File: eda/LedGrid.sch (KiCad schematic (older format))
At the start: 99 parts

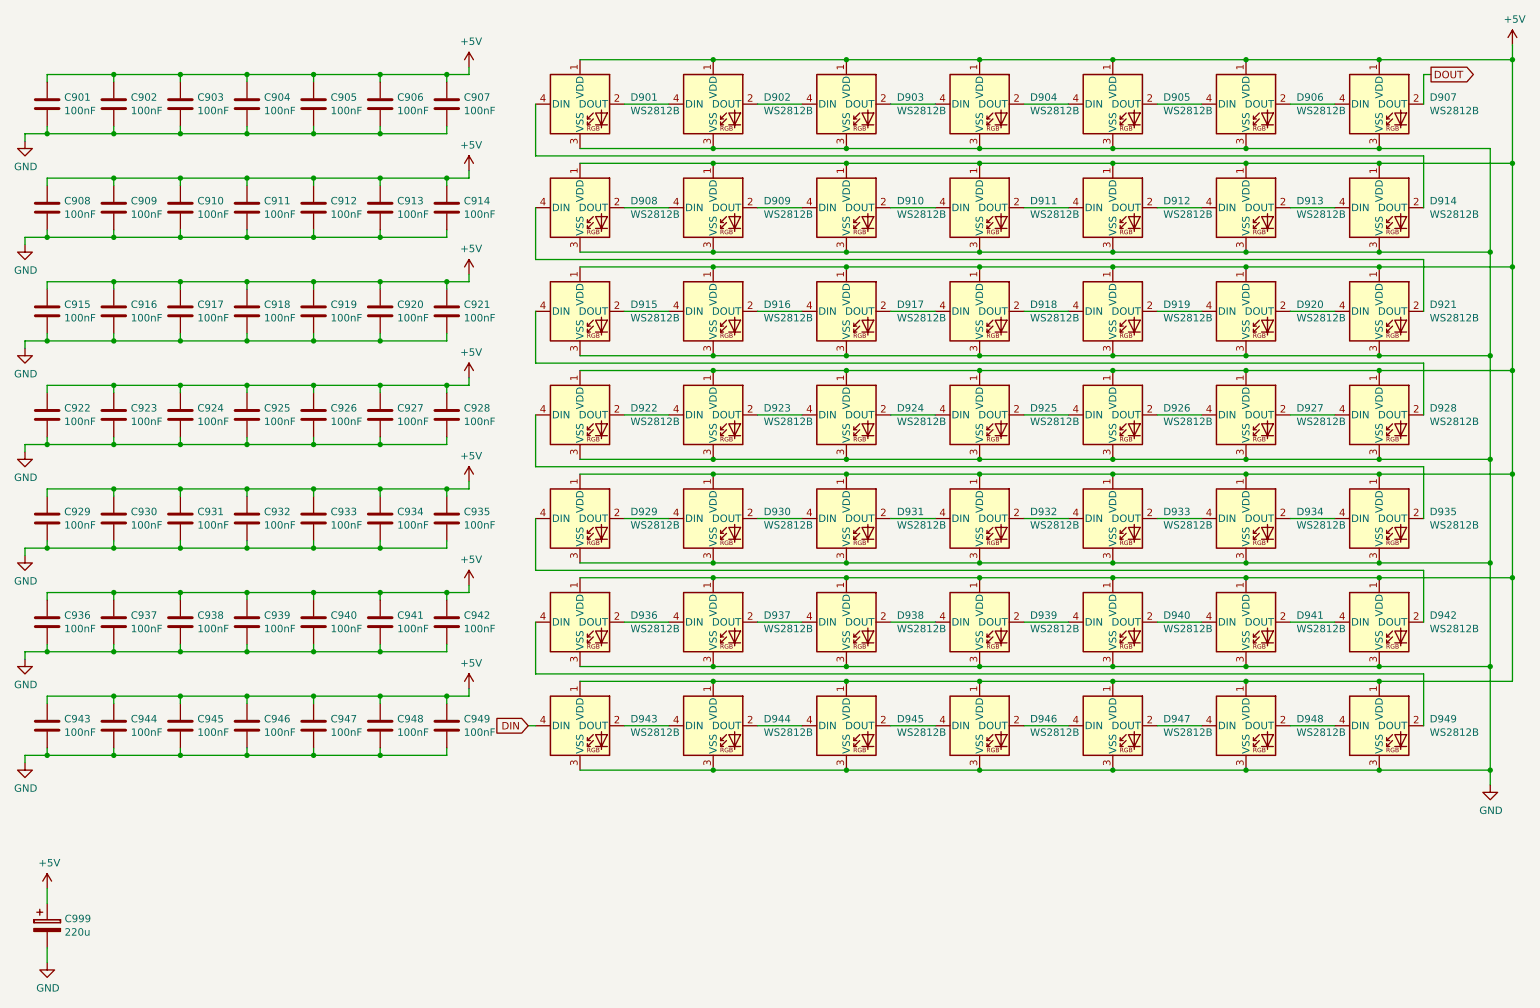
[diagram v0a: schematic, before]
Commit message: WS2812B grid finished
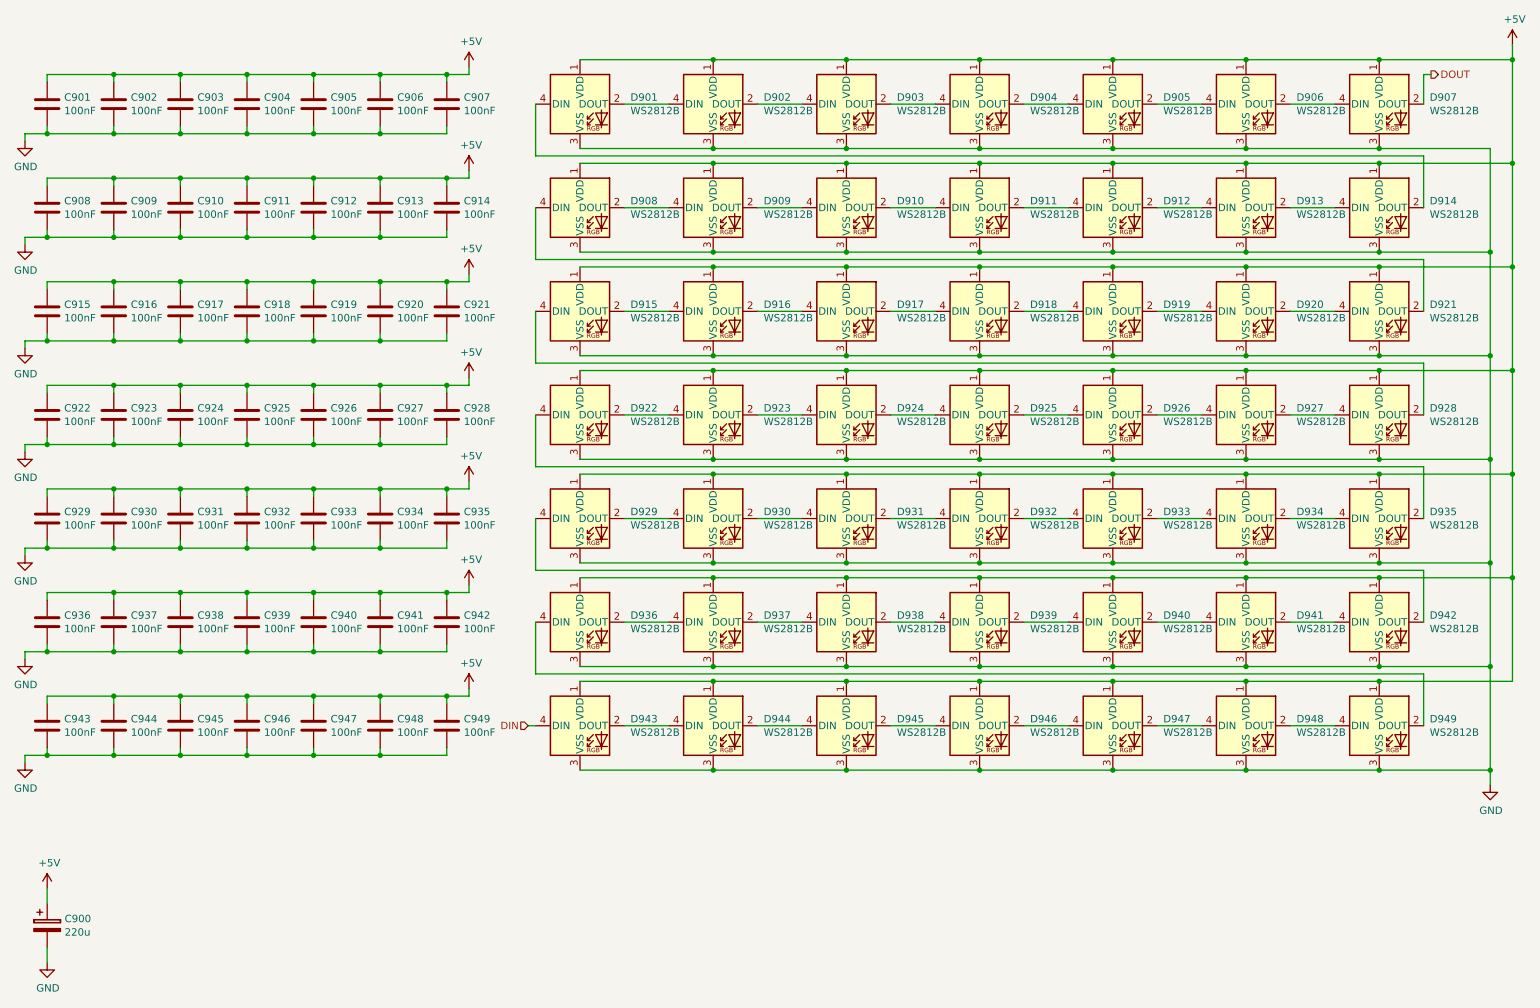
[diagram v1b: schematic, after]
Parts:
- C902, C903, C904, C905, C906, C907, C908, C909, C910, C911, C912, C913, C914, C915, C916, C917, C918, C919, C920, C921, C922, C923, C924, C925, C926, C927, C928, C929, C930, C931, C932, C933, C934, C935, C936, C937, C938, C939, C940, C941, C942, C943, C944, C945, C946, C947, C948, C949: footprint Capacitor_SMD:CP_Elec_6.3x5.3 -> Capacitor_SMD:C_0603_1608Metric
- renumbered C999 to C900

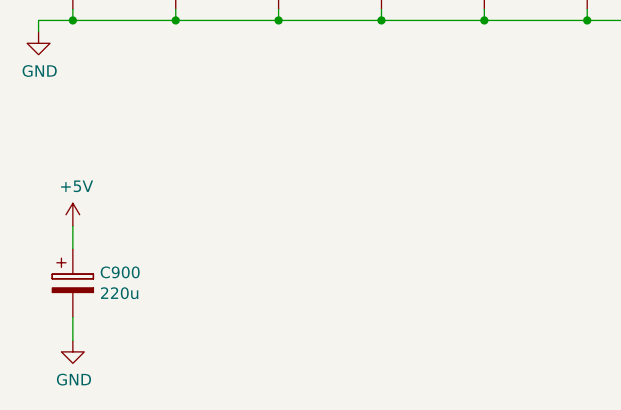
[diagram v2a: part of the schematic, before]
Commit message: silk screen documentation added
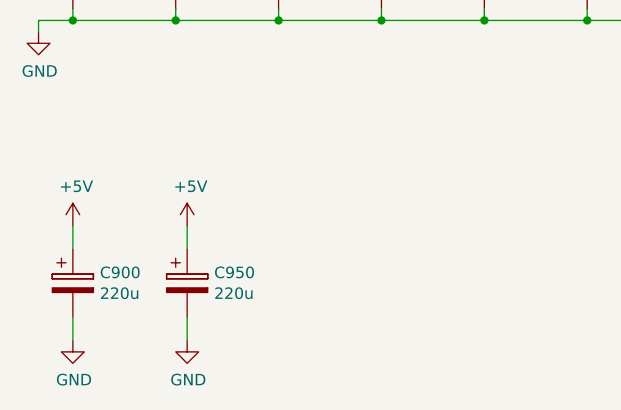
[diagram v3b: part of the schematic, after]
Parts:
- added C950: 220u, Capacitor_SMD:CP_Elec_6.3x5.3, symbol Device:CP
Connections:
- net +5V: now also C950.1
- net GND: now also C950.2
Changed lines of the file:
@@
 Text HLabel 10350 1200 2    50   Output ~ 0
 DOUT
+$Comp
+L power:+5V #PWR0131
+U 1 1 5C168154
+P 1500 6700
+F 0 "#PWR0131" H 1500 6550 50  0001 C CNN
+F 1 "+5V" H 1515 6873 50  0000 C CNN
+F 2 "" H 1500 6700 50  0001 C CNN
+F 3 "" H 1500 6700 50  0001 C CNN
+	1    1500 6700
+	1    0    0    -1
+$EndComp
+$Comp
+L power:GND #PWR0132
+U 1 1 5C16815A
+P 1500 7200
+F 0 "#PWR0132" H 1500 6950 50  0001 C CNN
+F 1 "GND" H 1505 7027 50  0000 C CNN
+F 2 "" H 1500 7200 50  0001 C CNN
+F 3 "" H 1500 7200 50  0001 C CNN
+	1    1500 7200
+	1    0    0    -1
+$EndComp
+$Comp
+L Device:CP C950
+U 1 1 5C168160
+P 1500 6950
+F 0 "C950" H 1618 6996 50  0000 L CNN
+F 1 "220u" H 1618 6905 50  0000 L CNN
+F 2 "Capacitor_SMD:CP_Elec_6.3x5.3" H 1538 6800 50  0001 C CNN
+F 3 "~" H 1500 6950 50  0001 C CNN
+	1    1500 6950
+	1    0    0    -1
+$EndComp
+Wire Wire Line
+	1500 6700 1500 6800
+Wire Wire Line
+	1500 7100 1500 7200
 $EndSCHEMATC
